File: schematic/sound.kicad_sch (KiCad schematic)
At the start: 18 parts, among them J2 Conn_01x02, J9 SJ1-3525NG, U1 LM386, U11 YMZ284, U2 SN76489AN

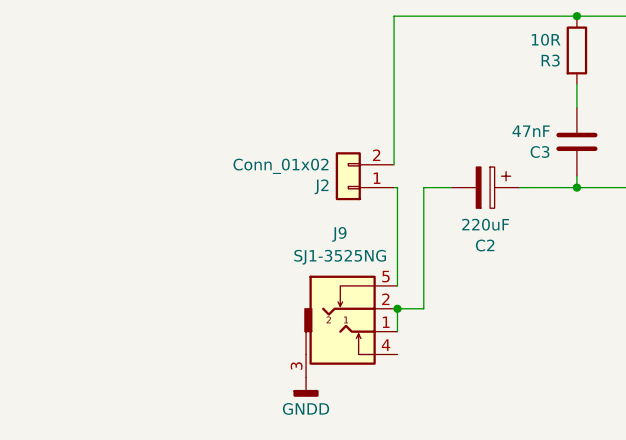
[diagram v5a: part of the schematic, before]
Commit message: updated output jacks to correct footprint
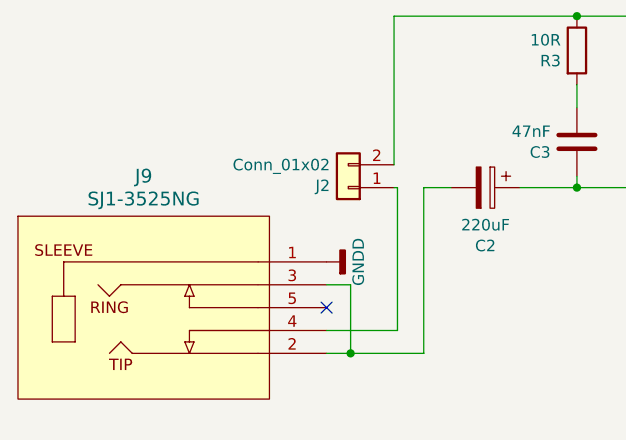
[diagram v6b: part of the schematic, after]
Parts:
- removed J9: SJ1-3525NG, jacks:spc21348, symbol jacks:eighth_inch_jack
- added J9: SJ1-3525NG, jacks2:SJ1-3525NG_CUD, symbol SJ-63053A:SJ1-3525NG
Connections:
- net GNDD: now also J9.1
- net at C2.2: now also J9.2, J9.3
- net at J2.1 (Pin_1): now also J9.4
- no-connect marks 3 -> 4
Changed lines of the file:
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@@
   (junction (at 109.093 46.101) (diameter 0) (color 0 0 0 0)
   )
-  (junction (at 75.819 120.142) (diameter 0) (color 0 0 0 0)
+  (junction (at 70.612 125.095) (diameter 0) (color 0 0 0 0)
   )
   (junction (at 139.192 101.6) (diameter 0) (color 0 0 0 0)
@@
   )
   (no_connect (at 112.141 99.06))
+  (no_connect (at 67.945 120.015))
   (no_connect (at 112.141 114.3))
   (no_connect (at 109.601 99.06))
@@
     (stroke (width 0) (type default))
   )
-  (wire (pts (xy 78.74 106.68) (xy 78.74 120.142))
+  (wire (pts (xy 78.74 106.68) (xy 78.74 125.095))
     (stroke (width 0) (type default))
   )
@@
     (stroke (width 0) (type default))
   )
-  (wire (pts (xy 75.819 120.142) (xy 75.819 122.682))
-    (stroke (width 0) (type default))
-  )
   (wire (pts (xy 99.822 53.721) (xy 109.093 53.721))
     (stroke (width 0) (type default))
@@
     (stroke (width 0) (type default))
   )
+  (wire (pts (xy 67.945 122.555) (xy 75.819 122.555))
+    (stroke (width 0) (type default))
+  )
   (bus (pts (xy 204.216 39.878) (xy 204.216 42.418))
     (stroke (width 0) (type default))
@@
     (stroke (width 0) (type default))
   )
-  (wire (pts (xy 75.819 117.602) (xy 75.819 106.68))
-    (stroke (width 0) (type default))
-  )
   (wire (pts (xy 109.093 53.721) (xy 118.999 53.721))
     (stroke (width 0) (type default))
@@
     (stroke (width 0) (type default))
   )
+  (wire (pts (xy 70.612 117.475) (xy 70.612 125.095))
+    (stroke (width 0) (type default))
+  )
   (bus (pts (xy 204.216 100.33) (xy 204.216 102.87))
     (stroke (width 0) (type default))
   )
-  (wire (pts (xy 78.74 120.142) (xy 75.819 120.142))
-    (stroke (width 0) (type default))
-  )
   (wire (pts (xy 173.482 30.988) (xy 175.006 30.988))
     (stroke (width 0) (type default))
@@
     (stroke (width 0) (type default))
   )
+  (wire (pts (xy 70.612 125.095) (xy 67.945 125.095))
+    (stroke (width 0) (type default))
+  )
   (bus (pts (xy 204.216 42.418) (xy 204.216 44.958))
     (stroke (width 0) (type default))
   )
+  (wire (pts (xy 67.945 117.475) (xy 70.612 117.475))
+    (stroke (width 0) (type default))
+  )
   (wire (pts (xy 89.027 46.101) (xy 99.822 46.101))
     (stroke (width 0) (type default))
@@
     (stroke (width 0) (type default))
   )
+  (wire (pts (xy 75.819 106.68) (xy 75.819 122.555))
+    (stroke (width 0) (type default))
+  )
   (wire (pts (xy 95.758 87.63) (xy 75.438 87.63))
     (stroke (width 0) (type default))
@@
   )
   (wire (pts (xy 104.521 106.68) (xy 95.758 106.68))
+    (stroke (width 0) (type default))
+  )
+  (wire (pts (xy 78.74 125.095) (xy 70.612 125.095))
     (stroke (width 0) (type default))
   )
@@
     )
   )
-  (symbol (lib_id "power:GNDD") (at 65.659 127.762 0) (unit 1)
-    (in_bom yes) (on_board yes) (dnp no)
-    (property "Reference" "#PWR084" (at 65.659 134.112 0)
-      (effects (font (size 1.27 1.27)) hide)
-    )
-    (property "Value" "GNDD" (at 68.326 131.318 0)
+  (symbol (lib_id "power:GNDD") (at 67.945 114.935 90) (unit 1)
+    (in_bom yes) (on_board yes) (dnp no)
+    (property "Reference" "#PWR084" (at 74.295 114.935 0)
+      (effects (font (size 1.27 1.27)) hide)
+    )
+    (property "Value" "GNDD" (at 71.501 112.268 0)
       (effects (font (size 1.27 1.27)) (justify right))
     )
-    (property "Footprint" "" (at 65.659 127.762 0)
-      (effects (font (size 1.27 1.27)) hide)
-    )
-    (property "Datasheet" "" (at 65.659 127.762 0)
+    (property "Footprint" "" (at 67.945 114.935 0)
+      (effects (font (size 1.27 1.27)) hide)
+    )
+    (property "Datasheet" "" (at 67.945 114.935 0)
       (effects (font (size 1.27 1.27)) hide)
     )
@@
         (path "/970e0f64-111f-41e3-9f5a-fb0d0f6fa101/00000000-0000-0000-0000-000062624749"
           (reference "#PWR011") (unit 1)
-        )
-      )
-    )
-  )
-  (symbol (lib_id "jacks:eighth_inch_jack") (at 69.469 127.762 0) (unit 1)
-    (in_bom yes) (on_board yes) (dnp no) (fields_autoplaced)
-    (property "Reference" "J9" (at 69.469 111.76 0)
-      (effects (font (size 1.27 1.27)))
-    )
-    (property "Value" "SJ1-3525NG" (at 69.469 114.3 0)
-      (effects (font (size 1.27 1.27)))
-    )
-    (property "Footprint" "jacks:spc21348" (at 69.469 127.762 0)
-      (effects (font (size 1.27 1.27)) hide)
-    )
-    (property "Datasheet" "" (at 69.469 127.762 0)
-      (effects (font (size 1.27 1.27)) hide)
-    )
-    (pin "1")
-    (pin "4")
-    (pin "5")
-    (pin "2")
-    (pin "3")
-    (instances
-      (project "coleco_original"
-        (path "/970e0f64-111f-41e3-9f5a-fb0d0f6fa101/00000000-0000-0000-0000-000062624749"
-          (reference "J9") (unit 1)
         )
       )
@@
         )
       )
+    )
+  )
+  (symbol (lib_id "SJ-63053A:SJ1-3525NG") (at 67.945 114.935 0) (unit 1)
+    (in_bom yes) (on_board yes) (dnp no) (fields_autoplaced)
+    (property "Reference" "J9" (at 47.625 105.41 0)
+      (effects (font (size 1.524 1.524)))
+    )
+    (property "Value" "SJ1-3525NG" (at 47.625 107.95 0)
+      (effects (font (size 1.524 1.524)))
+    )
+    (property "Footprint" "jacks2:SJ1-3525NG_CUD" (at 66.675 107.315 0)
+      (effects (font (size 1.27 1.27) italic) hide)
+    )
+    (property "Datasheet" "SJ1-3525NG" (at 65.405 103.505 0)
+      (effects (font (size 1.27 1.27) italic) hide)
+    )
+    (pin "3")
+    (pin "4")
+    (pin "2")
+    (pin "5")
+    (pin "1")
+    (instances
+      (project "coleco_original"
+        (path "/970e0f64-111f-41e3-9f5a-fb0d0f6fa101/00000000-0000-0000-0000-000062624749"
+          (reference "J9") (unit 1)
+        )
+      )

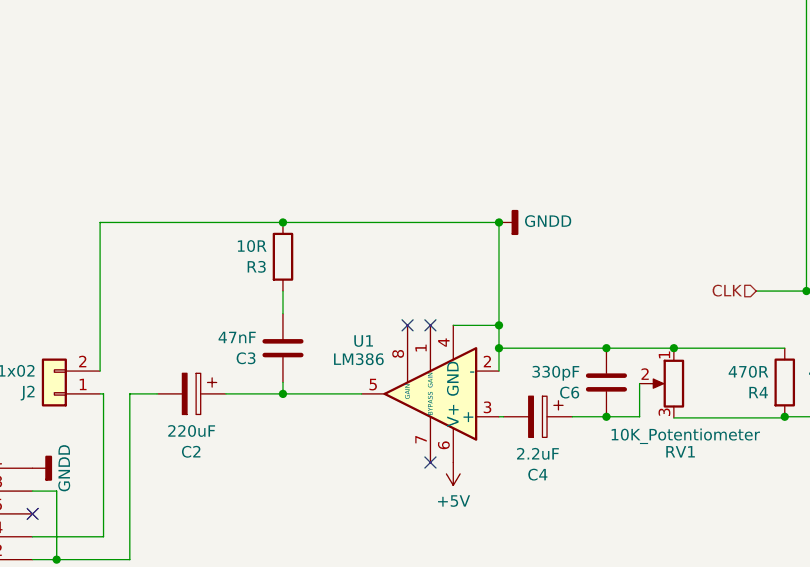
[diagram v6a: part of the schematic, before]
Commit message: change audio port so it does not conflict with volume knob
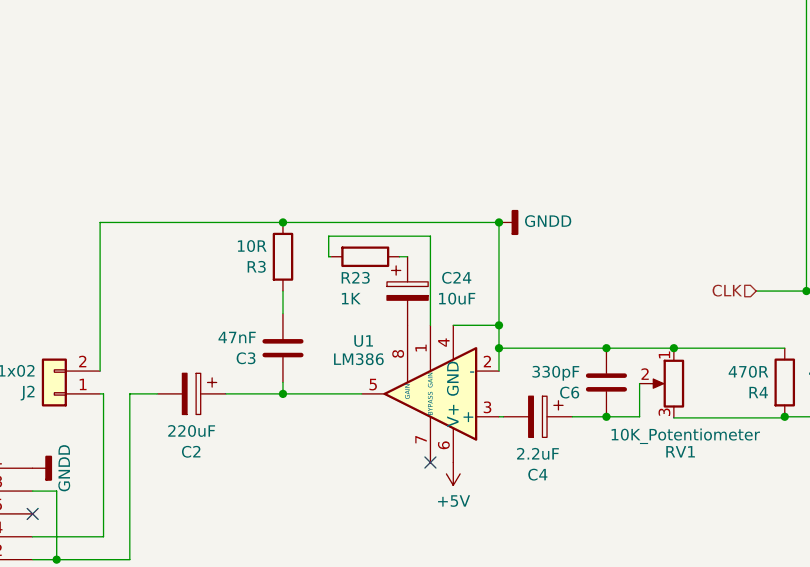
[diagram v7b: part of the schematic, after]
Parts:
- added C24: 10uF, Capacitor_THT:CP_Radial_D5.0mm_P2.50mm, symbol Device:CP
- added R23: 1K, Resistor_THT:R_Axial_DIN0207_L6.3mm_D2.5mm_P7.62mm_Horizontal, symbol Device:R
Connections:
- net at U1.1 (GAIN): now also R23.2
- net at U1.8 (GAIN): now also C24.2
- new net: C24.1, R23.1
- no-connect marks 4 -> 2
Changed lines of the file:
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@@
   (junction (at 175.006 116.84) (diameter 0) (color 0 0 0 0)
   )
-  (no_connect (at 112.141 99.06))
   (no_connect (at 67.945 120.015))
   (no_connect (at 112.141 114.3))
-  (no_connect (at 109.601 99.06))
   (bus_entry (at 201.676 105.41) (size 2.54 2.54)
     (stroke (width 0) (type default))
@@
     (stroke (width 0) (type default))
   )
+  (wire (pts (xy 100.838 91.44) (xy 101.092 91.44))
+    (stroke (width 0) (type default))
+  )
+  (wire (pts (xy 108.712 91.44) (xy 109.601 91.44))
+    (stroke (width 0) (type default))
+  )
   (wire (pts (xy 81.788 106.68) (xy 78.74 106.68))
     (stroke (width 0) (type default))
@@
     (stroke (width 0) (type default))
   )
+  (wire (pts (xy 100.838 89.154) (xy 100.838 91.44))
+    (stroke (width 0) (type default))
+  )
   (wire (pts (xy 173.482 30.988) (xy 175.006 30.988))
     (stroke (width 0) (type default))
@@
     (stroke (width 0) (type default))
   )
+  (wire (pts (xy 112.141 89.154) (xy 100.838 89.154))
+    (stroke (width 0) (type default))
+  )
   (wire (pts (xy 197.866 44.958) (xy 201.676 44.958))
     (stroke (width 0) (type default))
@@
   )
   (wire (pts (xy 139.192 101.727) (xy 139.192 101.6))
+    (stroke (width 0) (type default))
+  )
+  (wire (pts (xy 112.141 99.06) (xy 112.141 89.154))
     (stroke (width 0) (type default))
   )
@@
         (path "/970e0f64-111f-41e3-9f5a-fb0d0f6fa101/00000000-0000-0000-0000-000062624749"
           (reference "#PWR011") (unit 1)
+        )
+      )
+    )
+  )
+  (symbol (lib_id "Device:CP") (at 109.601 95.25 0) (unit 1)
+    (in_bom yes) (on_board yes) (dnp no)
+    (property "Reference" "C24" (at 115.062 93.8276 0)
+      (effects (font (size 1.27 1.27)))
+    )
+    (property "Value" "10uF" (at 115.062 96.139 0)
+      (effects (font (size 1.27 1.27)))
+    )
+    (property "Footprint" "Capacitor_THT:CP_Radial_D5.0mm_P2.50mm" (at 110.5662 99.06 0)
+      (effects (font (size 1.27 1.27)) hide)
+    )
+    (property "Datasheet" "~" (at 109.601 95.25 0)
+      (effects (font (size 1.27 1.27)) hide)
+    )
+    (pin "1")
+    (pin "2")
+    (instances
+      (project "coleco_original"
+        (path "/970e0f64-111f-41e3-9f5a-fb0d0f6fa101/00000000-0000-0000-0000-000062624749"
+          (reference "C24") (unit 1)
         )
       )
@@
         )
       )
+    )
+  )
+  (symbol (lib_id "Device:R") (at 104.902 91.44 270) (unit 1)
+    (in_bom yes) (on_board yes) (dnp no)
+    (property "Reference" "R23" (at 102.108 93.8276 90)
+      (effects (font (size 1.27 1.27)) (justify left))
+    )
+    (property "Value" "1K" (at 102.108 96.139 90)
+      (effects (font (size 1.27 1.27)) (justify left))
+    )
+    (property "Footprint" "Resistor_THT:R_Axial_DIN0207_L6.3mm_D2.5mm_P7.62mm_Horizontal" (at 104.902 89.662 90)
+      (effects (font (size 1.27 1.27)) hide)
+    )
+    (property "Datasheet" "~" (at 104.902 91.44 0)
+      (effects (font (size 1.27 1.27)) hide)
+    )
+    (pin "1")
+    (pin "2")
+    (instances
+      (project "coleco_original"
+        (path "/970e0f64-111f-41e3-9f5a-fb0d0f6fa101/00000000-0000-0000-0000-000062624749"
+          (reference "R23") (unit 1)
+        )
+      )

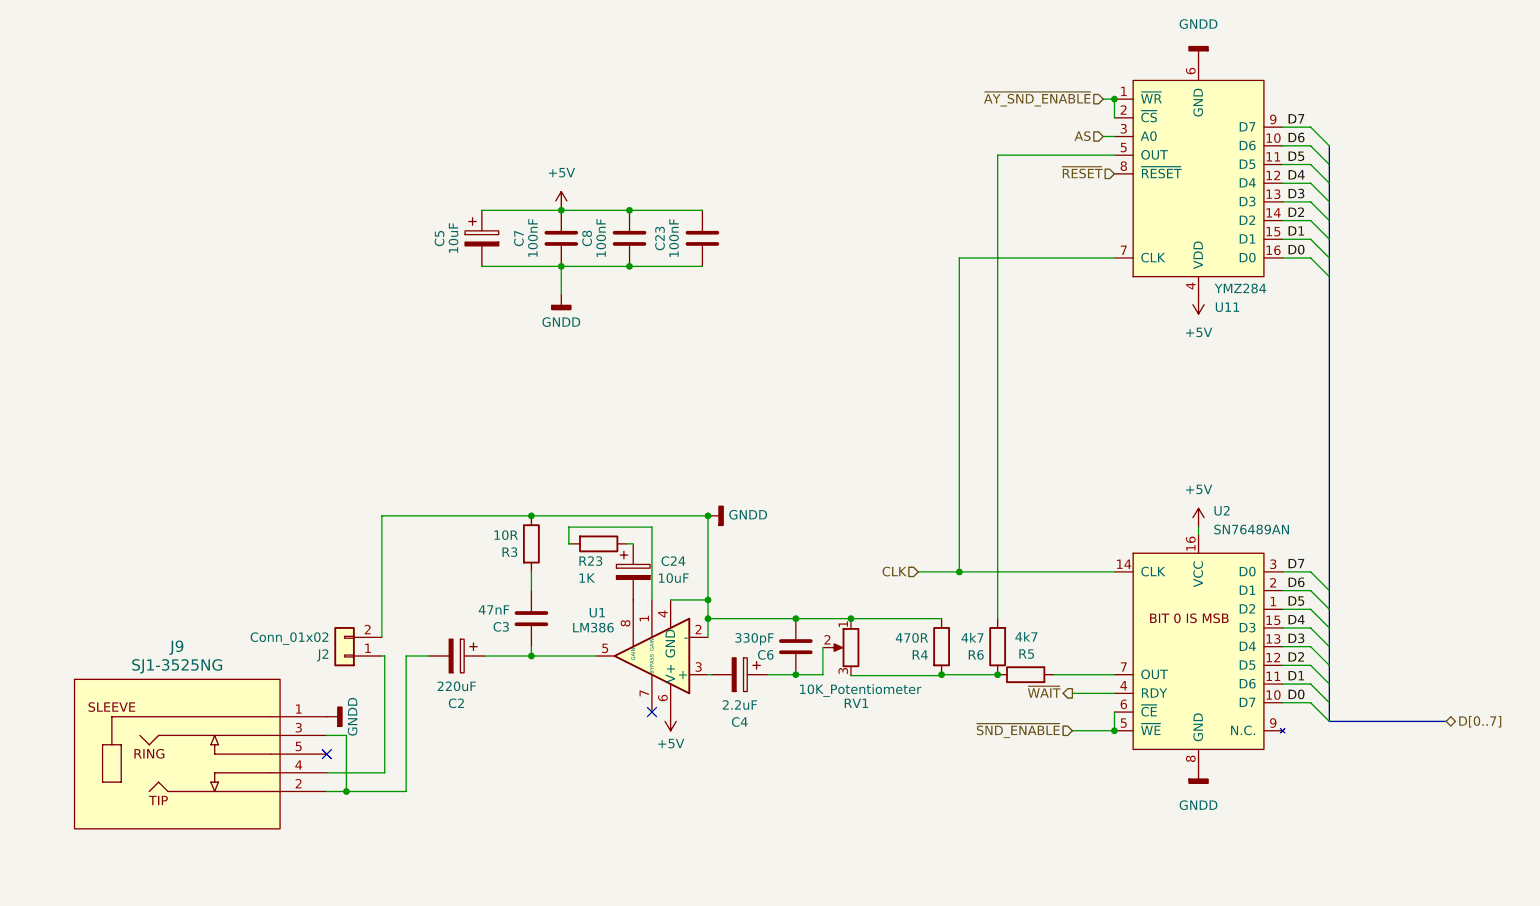
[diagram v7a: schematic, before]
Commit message: added new audio output amp, added choke to all audio path ICs. Tried to improve grounds
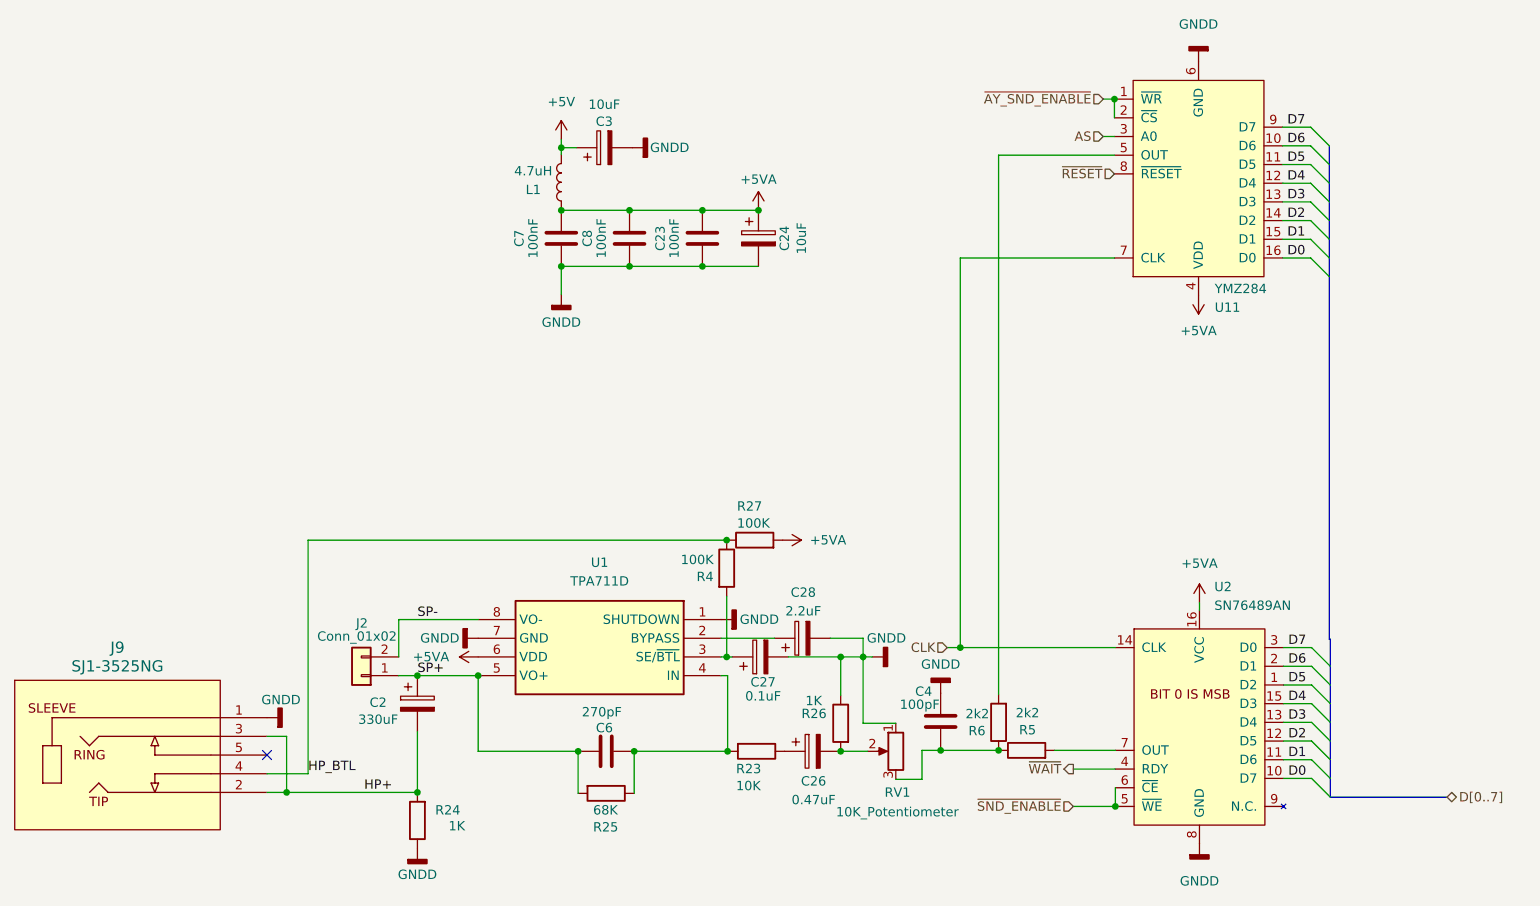
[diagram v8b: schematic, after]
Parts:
- removed C3: 47nF, Capacitor_THT:C_Disc_D4.7mm_W2.5mm_P5.00mm, symbol Device:C
- removed C4: 2.2uF, Capacitor_THT:CP_Radial_D5.0mm_P2.50mm, symbol Device:CP
- removed C5: 10uF, Capacitor_THT:CP_Radial_D5.0mm_P2.50mm, symbol Device:C_Polarized
- removed R3: 10R, Resistor_THT:R_Axial_DIN0207_L6.3mm_D2.5mm_P7.62mm_Horizontal, symbol Device:R
- removed U1: LM386, Package_DIP:DIP-8_W7.62mm, symbol Amplifier_Audio:LM386
- added C26: 0.47uF, Capacitor_THT:CP_Radial_D5.0mm_P2.00mm, symbol Device:C_Polarized
- added C27: 0.1uF, Capacitor_THT:CP_Radial_D5.0mm_P2.00mm, symbol Device:C_Polarized
- added C28: 2.2uF, Capacitor_THT:CP_Radial_D5.0mm_P2.00mm, symbol Device:C_Polarized
- added C3: 10uF, Capacitor_THT:CP_Radial_D5.0mm_P2.50mm, symbol Device:CP
- added C4: 100pF, Capacitor_THT:C_Disc_D4.7mm_W2.5mm_P5.00mm, symbol Device:C
- added L1: 4.7uH, Inductor_THT:L_Axial_L7.0mm_D3.3mm_P10.16mm_Horizontal_Fastron_MICC, symbol Device:L
- added R24, R26: 1K, Resistor_THT:R_Axial_DIN0207_L6.3mm_D2.5mm_P7.62mm_Horizontal, symbol Device:R
- added R25: 68K, Resistor_THT:R_Axial_DIN0207_L6.3mm_D2.5mm_P7.62mm_Horizontal, symbol Device:R
- added R27: 100K, Resistor_THT:R_Axial_DIN0207_L6.3mm_D2.5mm_P7.62mm_Horizontal, symbol Device:R
- added U1: TPA711D, TPA:SOIC127P600X175-8N, symbol TPA711D:TPA711D
- C2: value 220uF -> 330uF
- C6: value 330pF -> 270pF
- R23: value 1K -> 10K
- R4: value 470R -> 100K
- R5, R6: value 4k7 -> 2k2
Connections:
- net +5V: now also C3.1, L1.2; no longer C23.1, C7.1, C8.1, U11.4 (VDD), U2.16 (VCC)
- net GNDD: now also C24.2, C27.2, C28.2, C3.2, C4.1, R24.1, R26.1, U1.1 (SHUTDOWN), U1.7 (GND); no longer C6.1, J2.2 (Pin_2), R4.1
- net at R23.2: now also C6.2, R25.1, U1.4 (IN)
- net SP+: now reaches C2.1
- net SP+: now also C6.1, J2.1 (Pin_1), R25.2, U1.5 (VO+)
- net at R23.1: now also C26.1; no longer C24.1
- net at R5.1, R6.1, RV1.3: now also C4.2; no longer R4.2
- net at RV1.2: now also C26.2, R26.2; no longer C6.2
- net HP+: now reaches C2.2, J9.2, J9.3
- net HP+: now also R24.2
- net HP_BTL: now reaches J9.4
- net HP_BTL: now also R4.1, R27.1; no longer J2.1 (Pin_1)
- new net: C28.1, U1.2 (BYPASS)
- new net: C27.1, R4.2, U1.3 (SE/~{BTL})
- new net +5VA: C23.1, C24.1, C7.1, C8.1, L1.1, R27.2, U1.6 (VDD), U11.4 (VDD), U2.16 (VCC)
- new net SP-: J2.2 (Pin_2), U1.8 (VO-)
- no-connect marks 2 -> 1
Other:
- moved on the sheet: C2, C24, C6, J2, J9, R23, R4, R5, R6, RV1, U2
